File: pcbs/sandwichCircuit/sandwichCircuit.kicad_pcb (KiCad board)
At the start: 2 copper layers, 76 x 56 mm, 13 parts, among them IC1 3678, J5 Audio Out, U1 ESP32-DevKitC header, U2 CP2104 USB A board

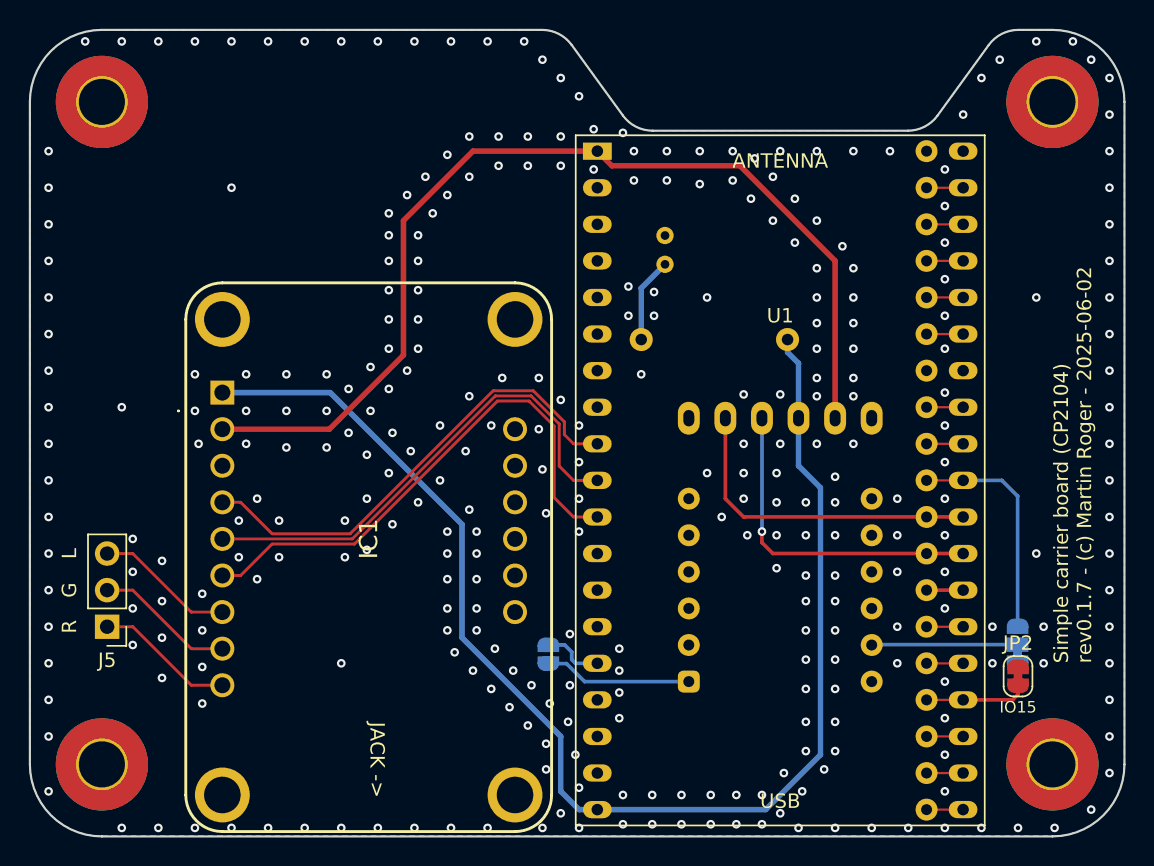
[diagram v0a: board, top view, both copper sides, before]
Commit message: SCB aligned to usage of S3
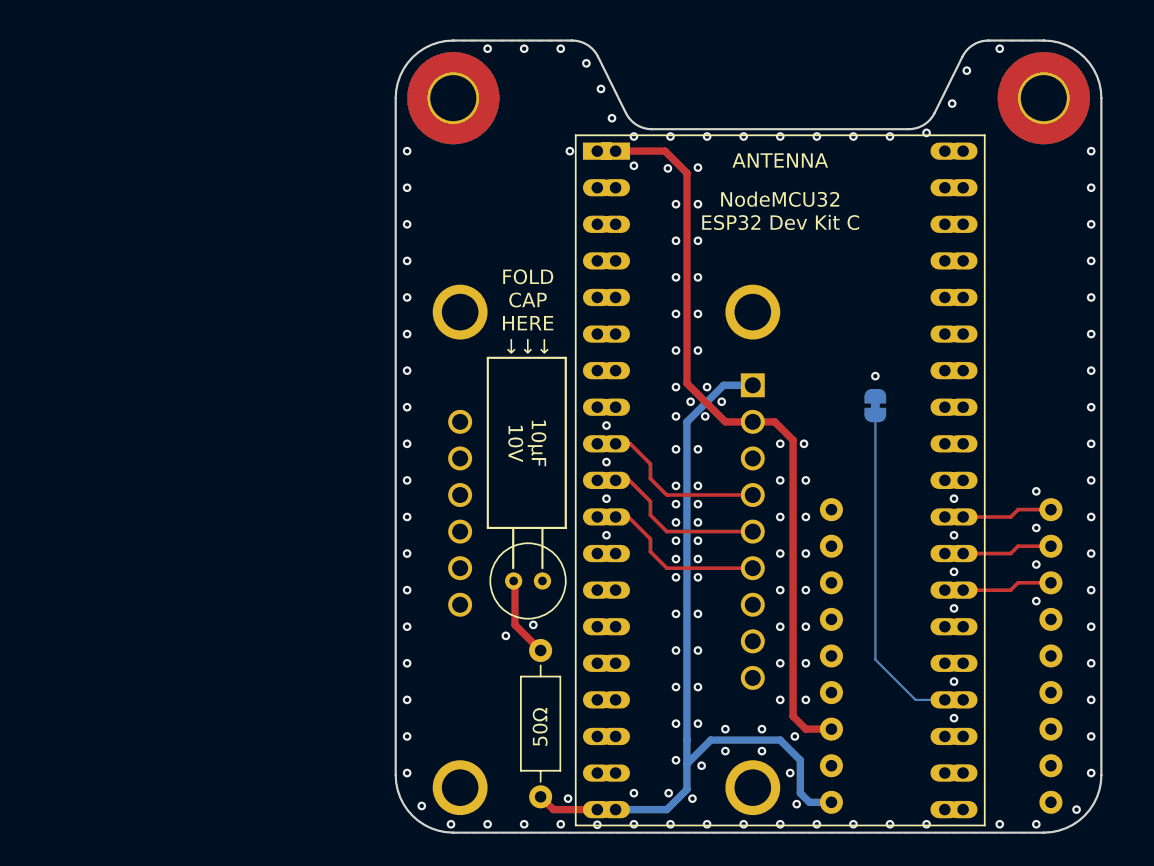
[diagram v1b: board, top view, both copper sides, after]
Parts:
- removed H3, H4: MountingHole_Pad, MountingHole:MountingHole_3.2mm_M3_Pad_TopBottom
- removed J5: Audio Out, Connector_PinHeader_2.54mm:PinHeader_1x03_P2.54mm_Vertical
- removed JP1: SolderJumper_3_Bridged12, Jumper:SolderJumper-3_P1.3mm_Bridged12_RoundedPad1.0x1.5mm
- removed JP3: SolderJumper_2_Open, Jumper:SolderJumper-2_P1.3mm_Open_RoundedPad1.0x1.5mm
- removed U2: CP2104 USB A board, DIY:CP2104_USB_Board
- added U3: ~, Project_parts:Waveshare ESP32 S3 Zero THT, B.Cu at (176.3, 93.5)
- C1, R1: moved to F.Cu
- H1: value MountingHole_Pad -> Mounting Hole
- H2: value MountingHole_Pad -> Mounting hole
- IC1: moved to B.Cu
- JP2: value SolderJumper_2_Bridged -> Silent Boot; moved to B.Cu
- moved IC1 36.8 mm to (163.2, 75.9)
- moved R1 36.1 mm to (148.5, 103.3), turned to 90 degrees
- moved H2 24.4 mm to (142.4, 54.7)
- moved C1 24.4 mm to (146.6, 88.3), turned to 0 degrees
- moved JP2 21.2 mm to (171.7, 76.1)
- moved H1 0.65 mm to (183.4, 54.7)
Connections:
- net GPIO15 renamed Net-(JP2-A)
- net GPIO25 renamed WSEL
- IC1 pad 7: LOUT -> unconnected-(IC1-LOUT-Pad7)
- IC1 pad 8: AGND -> unconnected-(IC1-AGND-Pad8)
- IC1 pad 9: ROUT -> unconnected-(IC1-ROUT-Pad9)
- U1 pad 15: GPIO13 -> unconnected-(U1-MTCK/GPIO13/ADC2_CH4-Pad15)
- U1 pad 20: CLK -> unconnected-(U1-SD_CLK/GPIO6-Pad20)
- U1 pad 21: D0 -> unconnected-(U1-SD_DATA0/GPIO7-Pad21)
- U1 pad 22: D1 -> unconnected-(U1-SD_DATA1/GPIO8-Pad22)_1
- U1 pad 24: GPIO2 -> unconnected-(U1-ADC2_CH2/GPIO2-Pad24)_1
- U1 pad 25: GPIO0 -> unconnected-(U1-GPIO0/BOOT/ADC2_CH1-Pad25)_1
- U1 pad 26: GPIO4 -> DCD
- U1 pad 27: GPIO16/U1RXD -> TXD
- U1 pad 28: GPIO17/U1TXD -> RXD
- U1 pad 29: GPIO5 -> unconnected-(U1-GPIO5-Pad29)_1
- U1 pad 30: GPIO18 -> unconnected-(U1-GPIO18-Pad30)
- U1 pad 31: GPIO19 -> unconnected-(U1-GPIO19-Pad31)_1
- U1 pad 33: GPIO21 -> unconnected-(U1-GPIO21-Pad33)_1
- U1 pad 34: GPIO3/U0RXD -> unconnected-(U1-U0RXD/GPIO3-Pad34)_1
- U1 pad 35: GPIO1/U0TXD -> unconnected-(U1-U0TXD/GPIO1-Pad35)_1
- U1 pad 36: GPIO22 -> unconnected-(U1-GPIO22-Pad36)
- U1 pad 37: GPIO23 -> unconnected-(U1-GPIO23-Pad37)
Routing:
- net +5V: track 91.2 -> 54.8 mm
- net BCLK: track 37.3 -> 11.5 mm
- net DIN: track 34.3 -> 11.6 mm
- net GPIO16/U1RXD: track 22.4 -> 0.00 mm, vias 1 -> 0
- net GPIO17/U1TXD: track 22.1 -> 0.00 mm
- net WSEL: track 33.1 -> 11.6 mm
- net +3.3V: track 70.6 -> 51.4 mm
- net Net-(JP2-A): track 7.11 -> 23.0 mm
- net GPIO5: track 15.8 -> 0.00 mm
- net RST: track 10.3 -> 0.00 mm
- net ROUT: track 9.68 -> 0.00 mm
- net LOUT: track 9.68 -> 0.00 mm
- net AGND: track 9.68 -> 0.00 mm
- net TXD: track 0.00 -> 6.31 mm
- net RXD: track 0.00 -> 6.31 mm
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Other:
- board size 76 x 56 mm -> 49 x 55 mm
- board text added: "${TITLE} rev${REVISION} (c) Martin Roger ${ISSUE_DATE}"
- board text added: "Adafruit 3678 UDA 1334A"
- board text added: "FOLD CAP HERE ↓↓↓"
- board text added: "NodeMCU32 ESP32 Dev Kit C"
- board text added: "Waveshare ESP32-S3-Zero"
- board text removed: "${TITLE} rev${REVISION} - (c) Martin Roger - ${ISSUE_DATE}"
- board text removed: "DCD"
- board text removed: "Fold capacitor ↓↓↓HERE↓↓↓"
- board text removed: "G"
- board text removed: "IO15"
- board text removed: "IO5"
- board text removed: "L"
- board text removed: "R"
- board text removed: "USB"
